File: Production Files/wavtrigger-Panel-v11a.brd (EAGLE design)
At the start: 147.8 x 139.7 mm, 451 parts, among them J1 5.5x2.1mm Barrel, J11 5.5x2.1mm Barrel, J13 USD-SOCKETNEW, J14 M02PTH, J16 M08X2, J18 M08X2, J19 M02PTH, J21 5.5x2.1mm Barrel, J23 USD-SOCKETNEW, J24 M02PTH, J26 M08X2, J28 M08X2, J29 M02PTH, J3 USD-SOCKETNEW, J31 5.5x2.1mm Barrel, J33 USD-SOCKETNEW, J34 M02PTH, J36 M08X2, J38 M08X2, J39 M02PTH, J5 M02PTH, J6 M08X2, J7 M08X2, J9 M02PTH, U11 STM32F405RG, U12 MIC5323-3.3, U13 PCM5100, U14 LM4990, U16 STM32F405RG, U17 MIC5323-3.3, U18 PCM5100, U19 LM4990, U2 MIC5323-3.3, U3 STM32F405RG, U4 STM32F405RG, U5 PCM5100, U6 LM4990, U7 MIC5323-3.3, U8 PCM5100, U9 LM4990, Y1 8MHz, Y2 8MHz, Y3 8MHz, Y4 8MHz

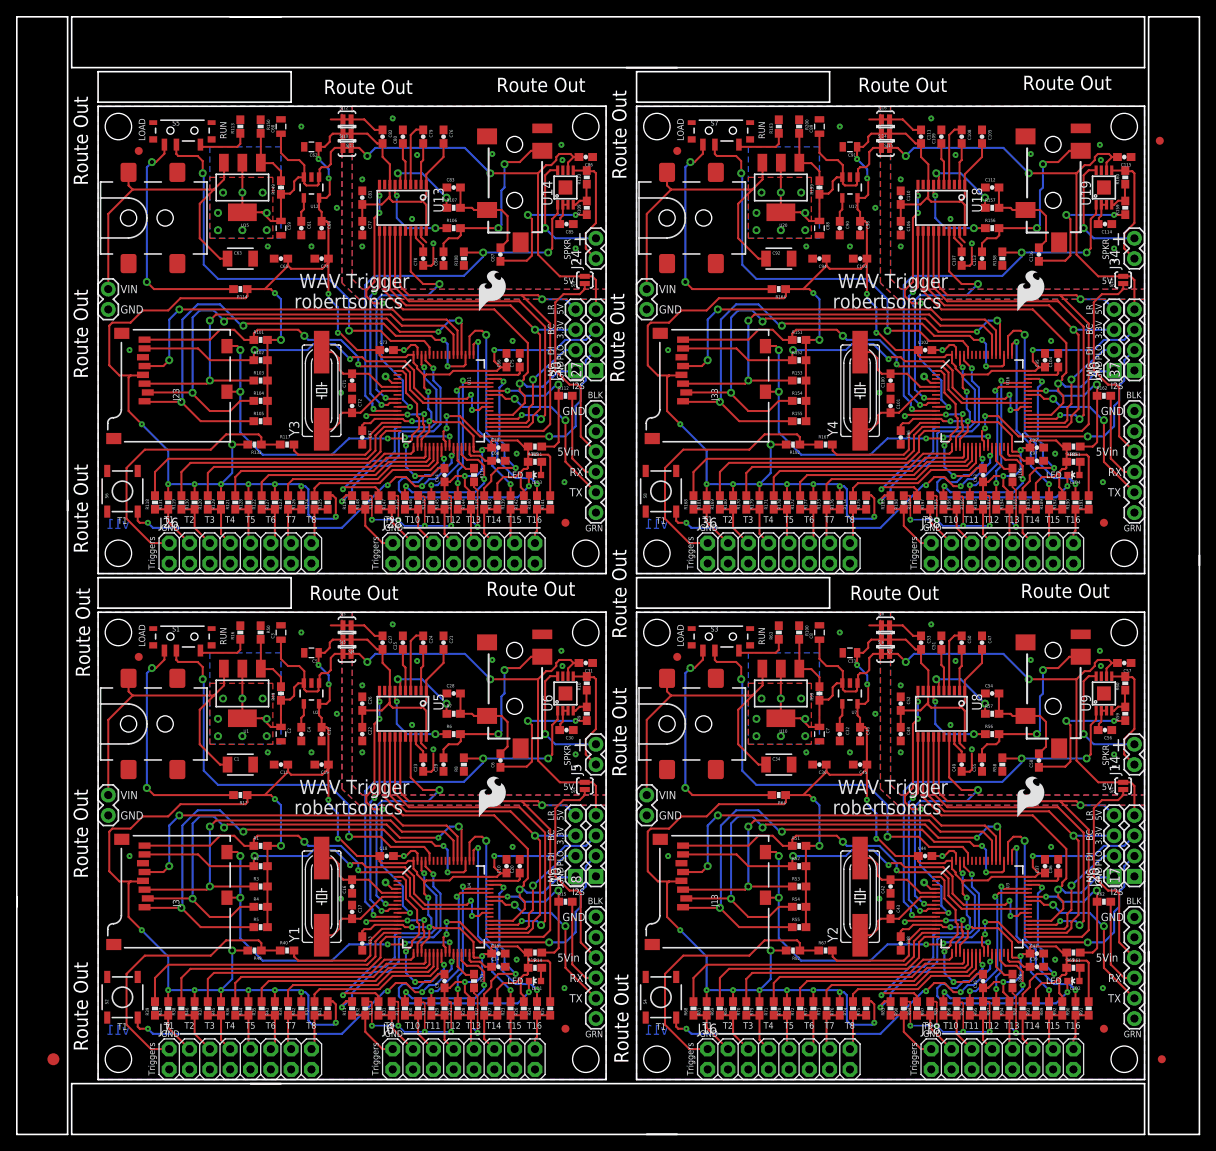
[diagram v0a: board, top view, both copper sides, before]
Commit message: re-did panel v11 for GP
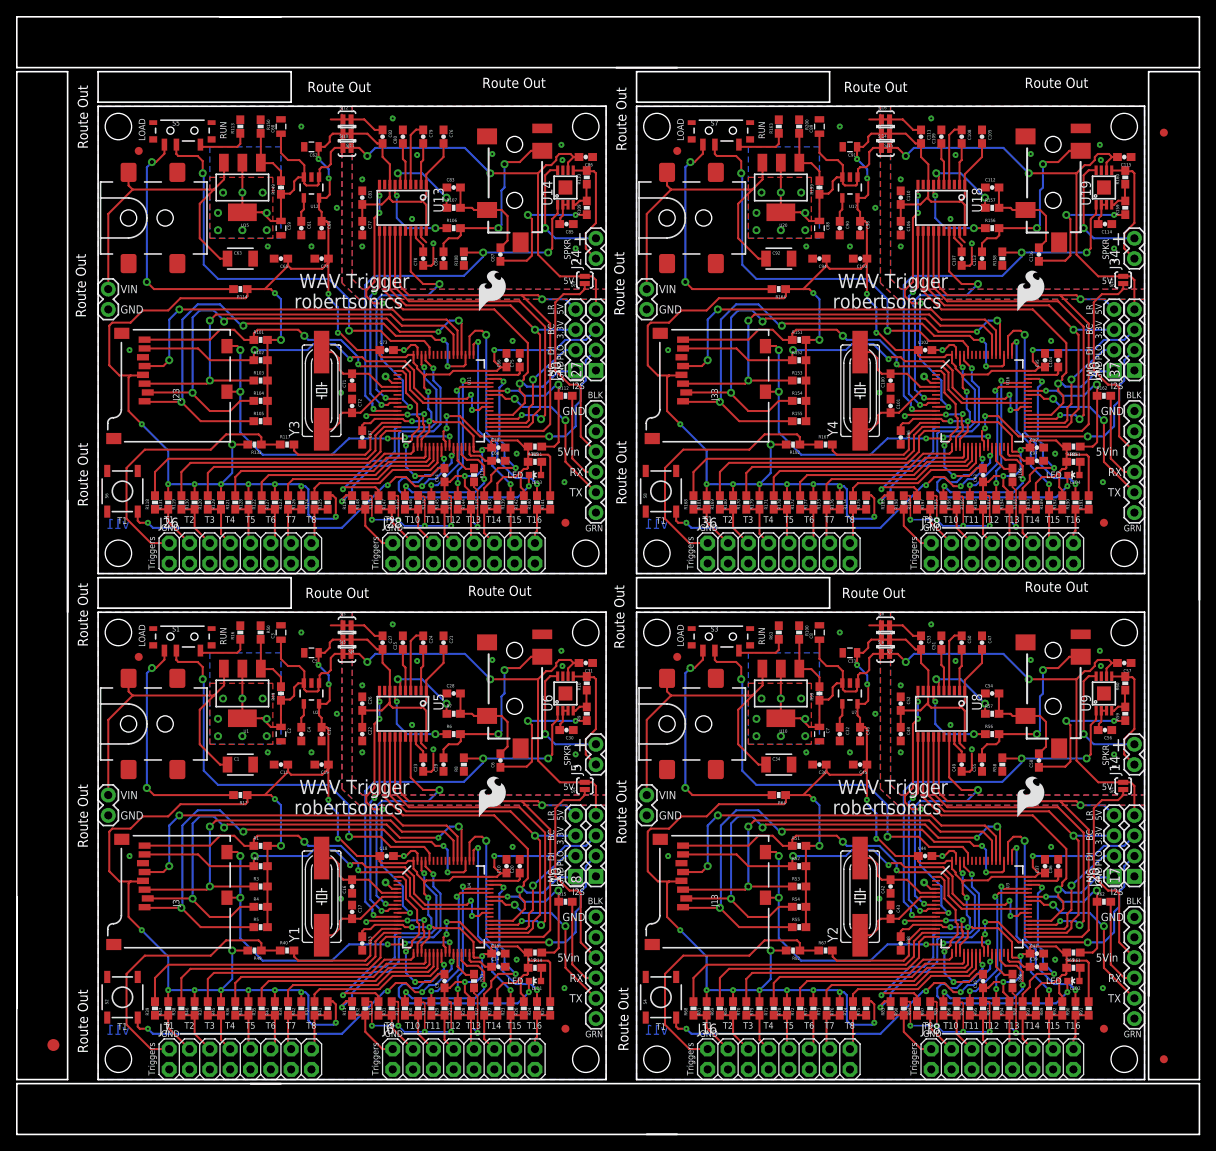
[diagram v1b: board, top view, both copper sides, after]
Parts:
- removed E$5, E$6: (no value), SparkFun-Aesthetics:FIDUCIAL-1X2
- added E$13, E$14: (no value), SparkFun-Aesthetics:FIDUCIAL-1X2
- moved E$1 1.78 mm to (4.57, 11.2)
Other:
- outline, holes or cut-outs redrawn
